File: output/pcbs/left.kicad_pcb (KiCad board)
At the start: 2 copper layers, 139.8 x 121.8 mm, 64 parts

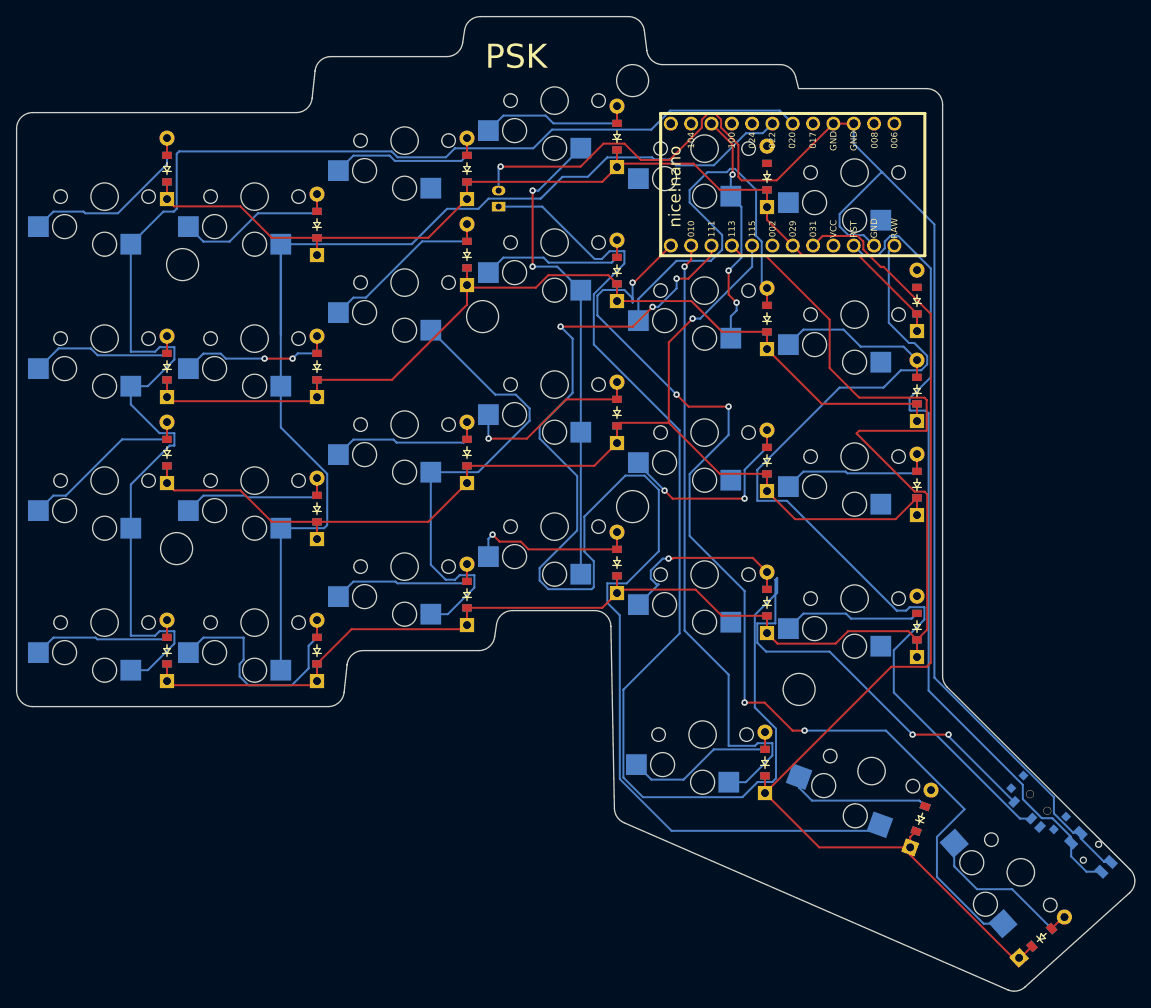
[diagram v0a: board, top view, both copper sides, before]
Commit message: clean slate, regenerated without trash routes
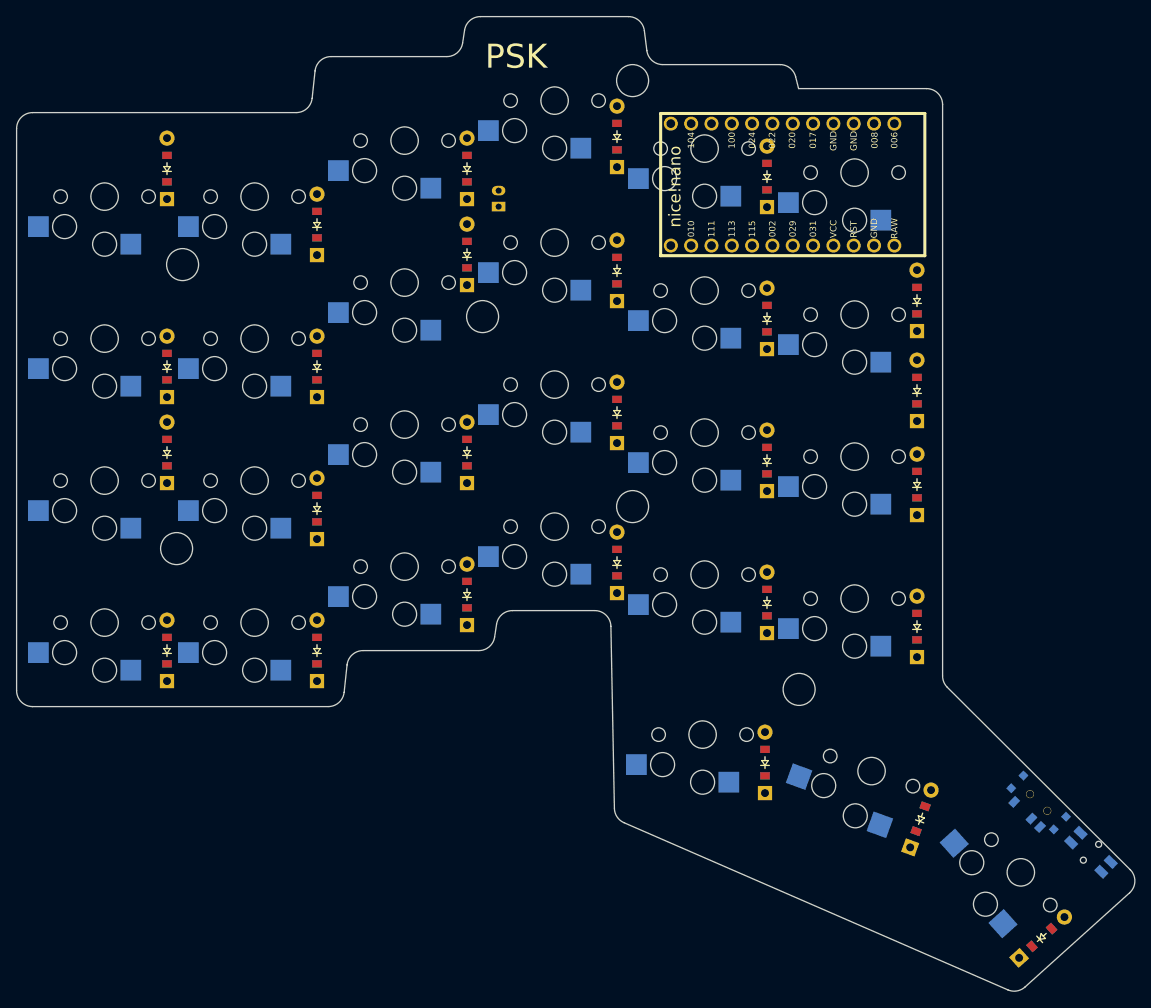
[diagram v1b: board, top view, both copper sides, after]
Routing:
- net pos: track 192.9 -> 0.00 mm, vias 2 -> 0
- net P113: track 192.4 -> 0.00 mm
- net GND: track 182.5 -> 0.00 mm, vias 1 -> 0
- net P020: track 173.7 -> 0.00 mm
- net P111: track 167.7 -> 0.00 mm, vias 3 -> 0
- net P115: track 144.3 -> 0.00 mm, vias 1 -> 0
- net P022: track 141.1 -> 0.00 mm
- net P031: track 138.5 -> 0.00 mm
- net P009: track 133.9 -> 0.00 mm, vias 5 -> 0
- net P029: track 119.5 -> 0.00 mm
- net P002: track 119.1 -> 0.00 mm
- net RAW: track 110.8 -> 0.00 mm
- net RST: track 102.8 -> 0.00 mm
- net P010: track 79.1 -> 0.00 mm, vias 1 -> 0
- net P100: track 60.5 -> 0.00 mm, vias 2 -> 0
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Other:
- outline, holes or cut-outs redrawn
- net class Default added: clearance 0.2, trace_width 0.25, via_dia 0.8, via_drill 0.4

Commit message: routed left, removed top left mounting hole from left and right and yaml
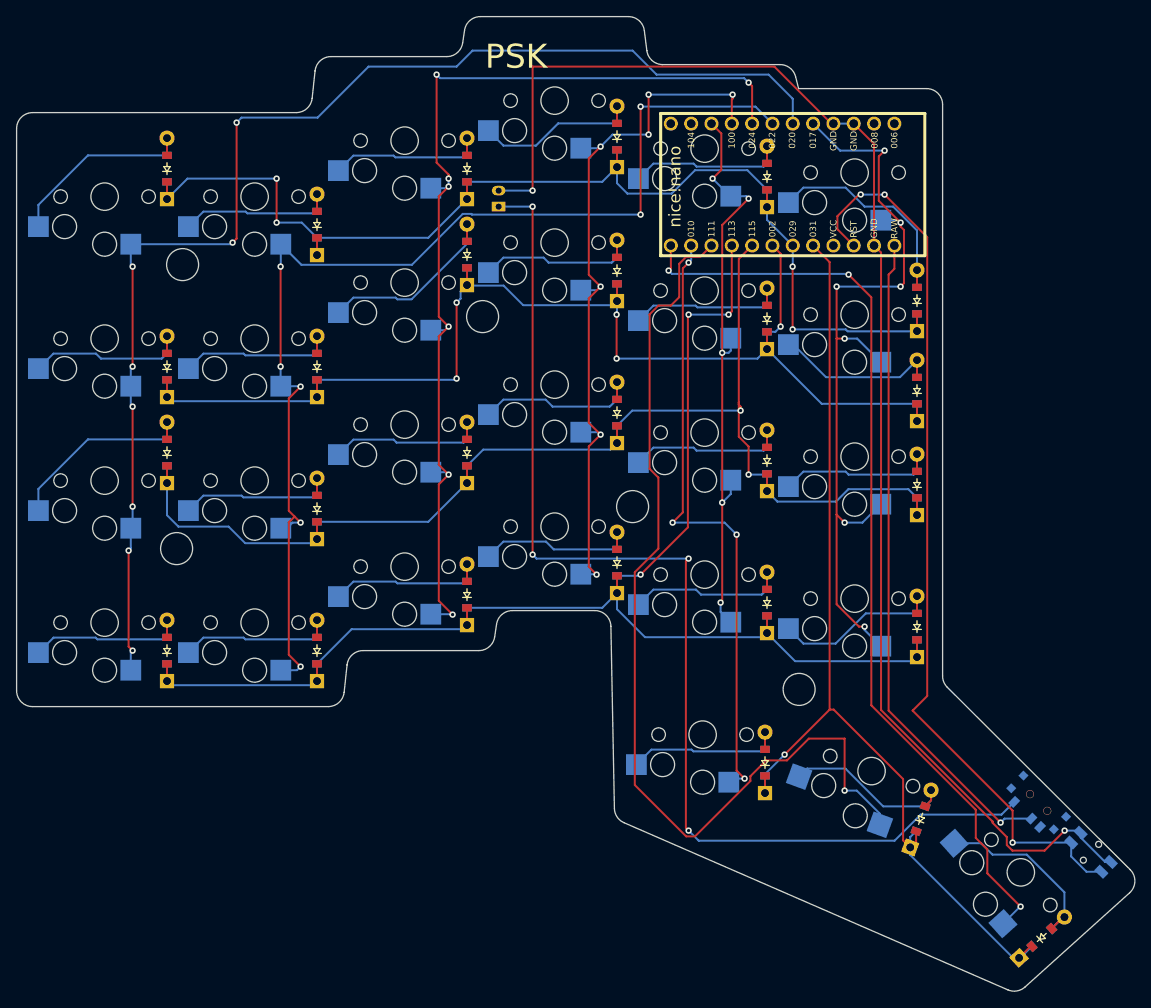
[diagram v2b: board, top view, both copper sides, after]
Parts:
- removed the ? at (166.0, 82.2)
- removed the ? at (186.8, 158.3)
- added ?: , HOLE_M2_TH, F.Cu at (186.8, 158.3)
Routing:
- net P113: track 0.00 -> 180.0 mm, vias 0 -> 3
- net GND: track 0.00 -> 177.2 mm, vias 0 -> 2
- net P115: track 0.00 -> 160.9 mm, vias 0 -> 2
- net P020: track 0.00 -> 160.9 mm, vias 0 -> 8
- net P002: track 0.00 -> 155.5 mm, vias 0 -> 5
- net P029: track 0.00 -> 148.1 mm, vias 0 -> 4
- net pos: track 0.00 -> 145.0 mm, vias 0 -> 4
- net P022: track 0.00 -> 143.2 mm, vias 0 -> 7
- net P024: track 0.00 -> 125.9 mm, vias 0 -> 7
- net P031: track 0.00 -> 125.5 mm, vias 0 -> 1
- net P111: track 0.00 -> 122.0 mm, vias 0 -> 1
- net P009: track 0.00 -> 116.9 mm, vias 0 -> 3
- net RST: track 0.00 -> 114.3 mm, vias 0 -> 3
- net P017: track 0.00 -> 101.0 mm, vias 0 -> 7
- net P100: track 0.00 -> 92.6 mm, vias 0 -> 7
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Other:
- outline, holes or cut-outs redrawn
- net class Default removed

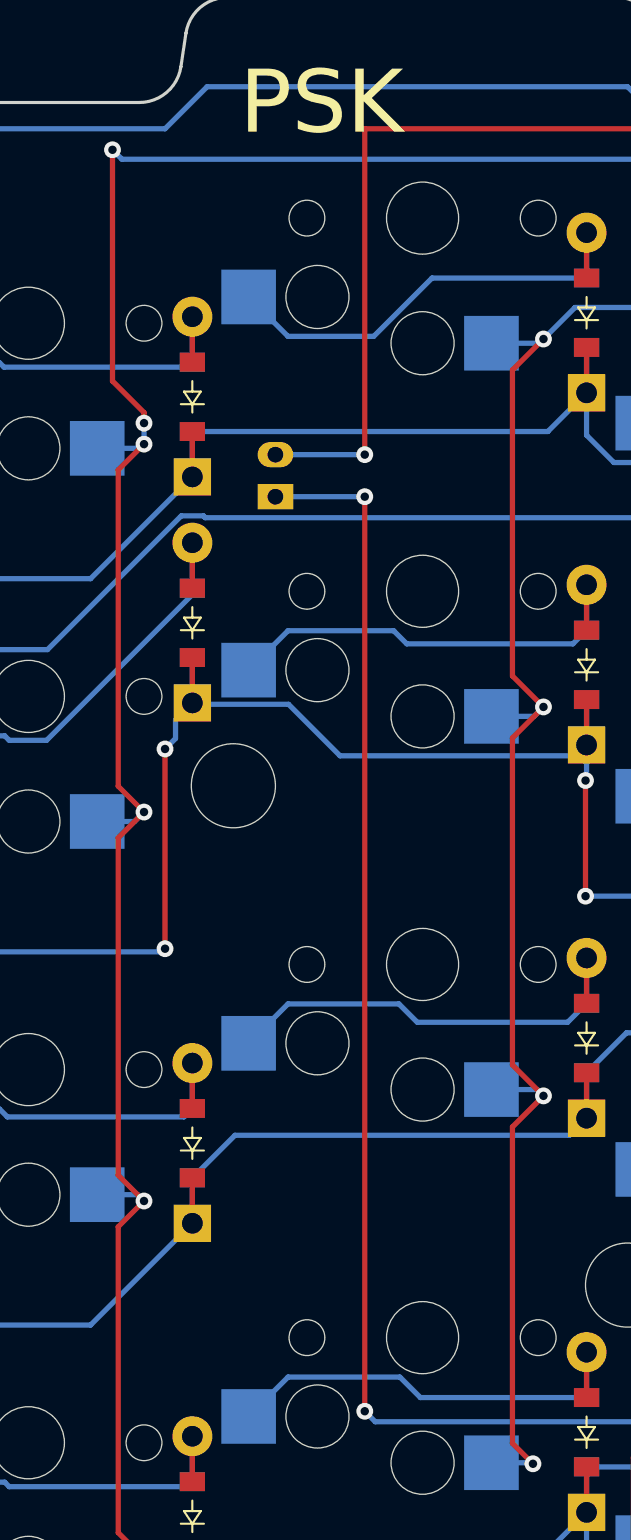
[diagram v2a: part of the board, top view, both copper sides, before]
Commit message: routed left and right, DRC passed
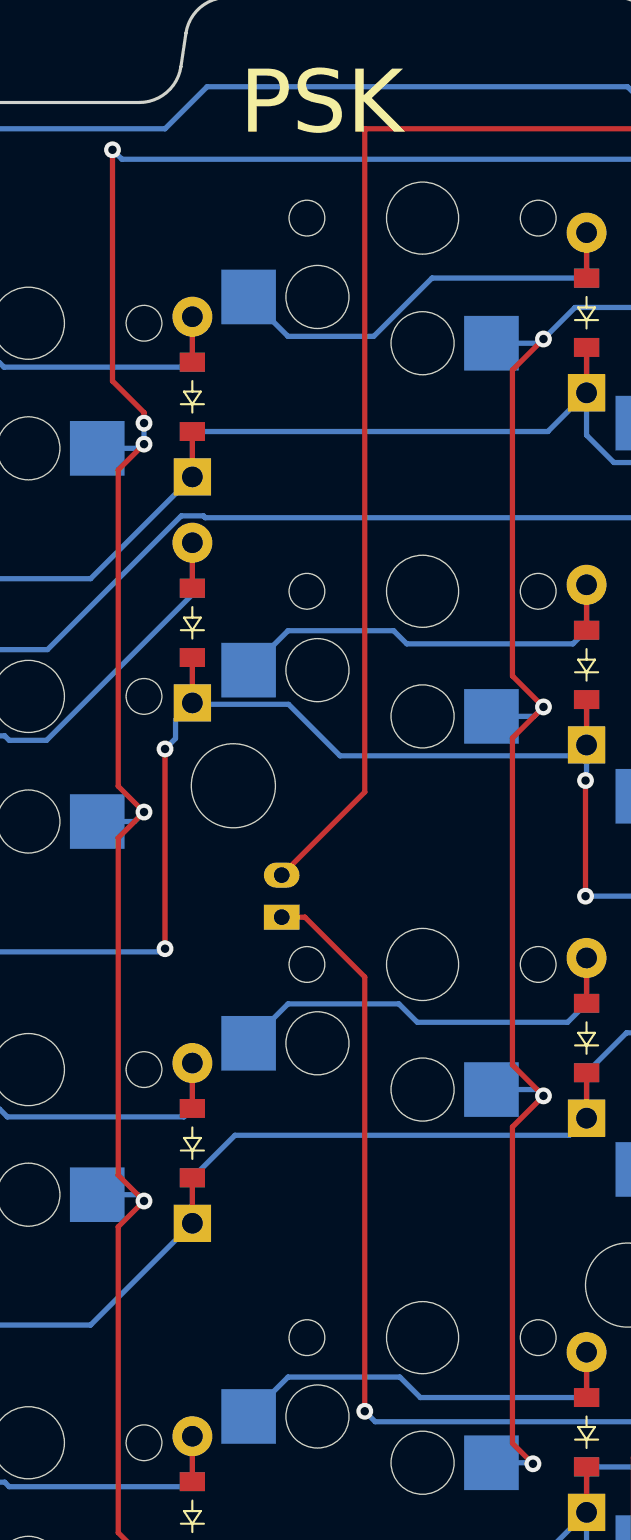
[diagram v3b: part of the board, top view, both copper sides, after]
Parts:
- moved JST1 20.0 mm to (149.6, 117.0)
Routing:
- net pos: track 145.0 -> 123.0 mm, vias 4 -> 3
- net GND: track 177.2 -> 194.6 mm, vias 2 -> 1
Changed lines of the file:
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@@
 	(footprint "JST_PH_S2B-PH-K_02x2.00mm_Angled"
 		(layer "F.Cu")
-		(at 149.25 97 90)
+		(at 149.55 117 90)
 		(descr "JST PH series connector, S2B-PH-K, side entry type, through hole, Datasheet: http://www.jst-mfg.com/product/pdf/eng/ePH.pdf")
 		(tags "connector jst ph")
@@
 	)
 	(segment
-		(start 183.717257 80.5)
-		(end 190.847257 87.63)
-		(width 0.25)
-		(layer "F.Cu")
-		(net 43)
-	)
-	(segment
 		(start 196.18 90.17)
 		(end 196.18 102.87)
@@
 	)
 	(segment
-		(start 153.5 96)
+		(start 153.5 112.05)
 		(end 153.5 80.5)
 		(width 0.25)
@@
 	)
 	(segment
-		(start 153.5 80.5)
-		(end 183.717257 80.5)
+		(start 183.717257 80.5)
+		(end 190.847257 87.63)
 		(width 0.25)
 		(layer "F.Cu")
@@
 	)
 	(segment
-		(start 211 174.863604)
-		(end 211 175.025305)
+		(start 149.55 116)
+		(end 153.5 112.05)
 		(width 0.25)
 		(layer "F.Cu")
@@
 	)
 	(segment
-		(start 212.775 177.800305)
-		(end 213.474695 178.5)
+		(start 153.5 80.5)
+		(end 183.717257 80.5)
 		(width 0.25)
 		(layer "F.Cu")
@@
 	)
 	(segment
-		(start 211 175.025305)
-		(end 212.775 176.800305)
+		(start 190.847257 87.63)
+		(end 191.1 87.63)
 		(width 0.25)
 		(layer "F.Cu")
@@
 	)
 	(segment
-		(start 190.847257 87.63)
-		(end 191.1 87.63)
+		(start 211 174.863604)
+		(end 211 175.025305)
 		(width 0.25)
 		(layer "F.Cu")
 		(net 43)
 	)
-	(via
-		(at 220 176)
-		(size 0.8)
-		(drill 0.4)
-		(layers "F.Cu" "B.Cu")
+	(segment
+		(start 212.775 177.800305)
+		(end 213.474695 178.5)
+		(width 0.25)
+		(layer "F.Cu")
+		(net 43)
+	)
+	(segment
+		(start 211 175.025305)
+		(end 212.775 176.800305)
+		(width 0.25)
+		(layer "F.Cu")
 		(net 43)
 	)
 	(via
-		(at 153.5 96)
+		(at 220 176)
 		(size 0.8)
 		(drill 0.4)
@@
 	)
 	(segment
-		(start 149.25 96)
-		(end 153.5 96)
-		(width 0.25)
-		(layer "B.Cu")
-		(net 43)
-	)
-	(segment
 		(start 191.1 87.63)
 		(end 193.64 87.63)
@@
 	)
 	(segment
-		(start 153.5 98)
-		(end 153.5 141.5)
+		(start 150.65 118)
+		(end 149.55 118)
 		(width 0.25)
 		(layer "F.Cu")
@@
 	)
 	(segment
+		(start 153.5 141.5)
+		(end 153.5 120.85)
+		(width 0.25)
+		(layer "F.Cu")
+		(net 50)
+	)
+	(segment
+		(start 153.5 120.85)
+		(end 150.65 118)
+		(width 0.25)
+		(layer "F.Cu")
+		(net 50)
+	)
+	(segment
 		(start 173 142)
 		(end 172.6605 142.3395)
@@
 	)
 	(via
-		(at 153.5 98)
-		(size 0.8)
-		(drill 0.4)
-		(layers "F.Cu" "B.Cu")
-		(net 50)
-	)
-	(via
 		(at 153.5 141.5)
 		(size 0.8)
@@
 		(width 0.25)
 		(layer "B.Cu")
-		(net 50)
-	)
-	(segment
-		(start 149.25 98)
-		(end 153.5 98)
-		(width 0.25)
-		(layer "B.Cu")

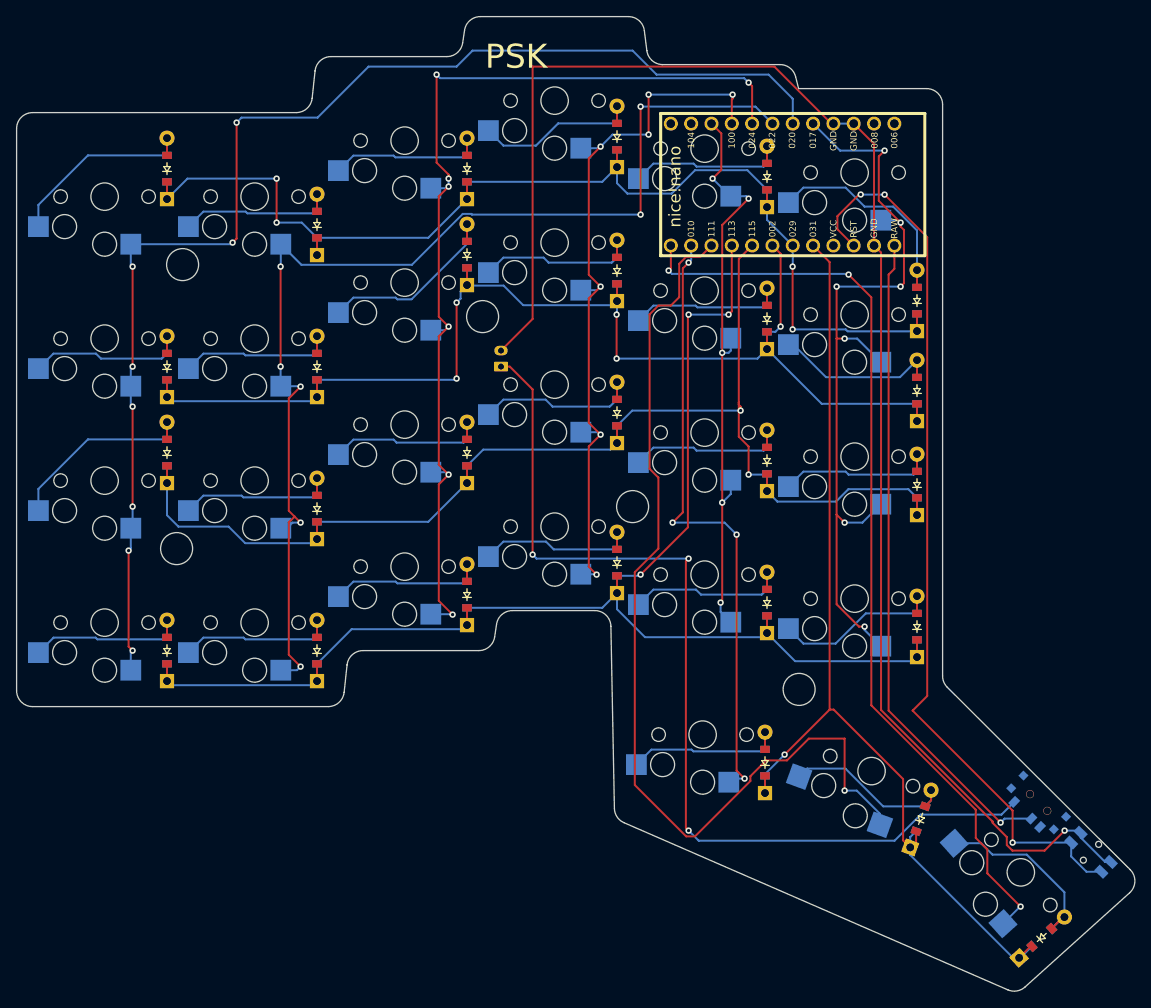
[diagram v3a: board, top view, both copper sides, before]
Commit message: generated gerber files, sent off for fab
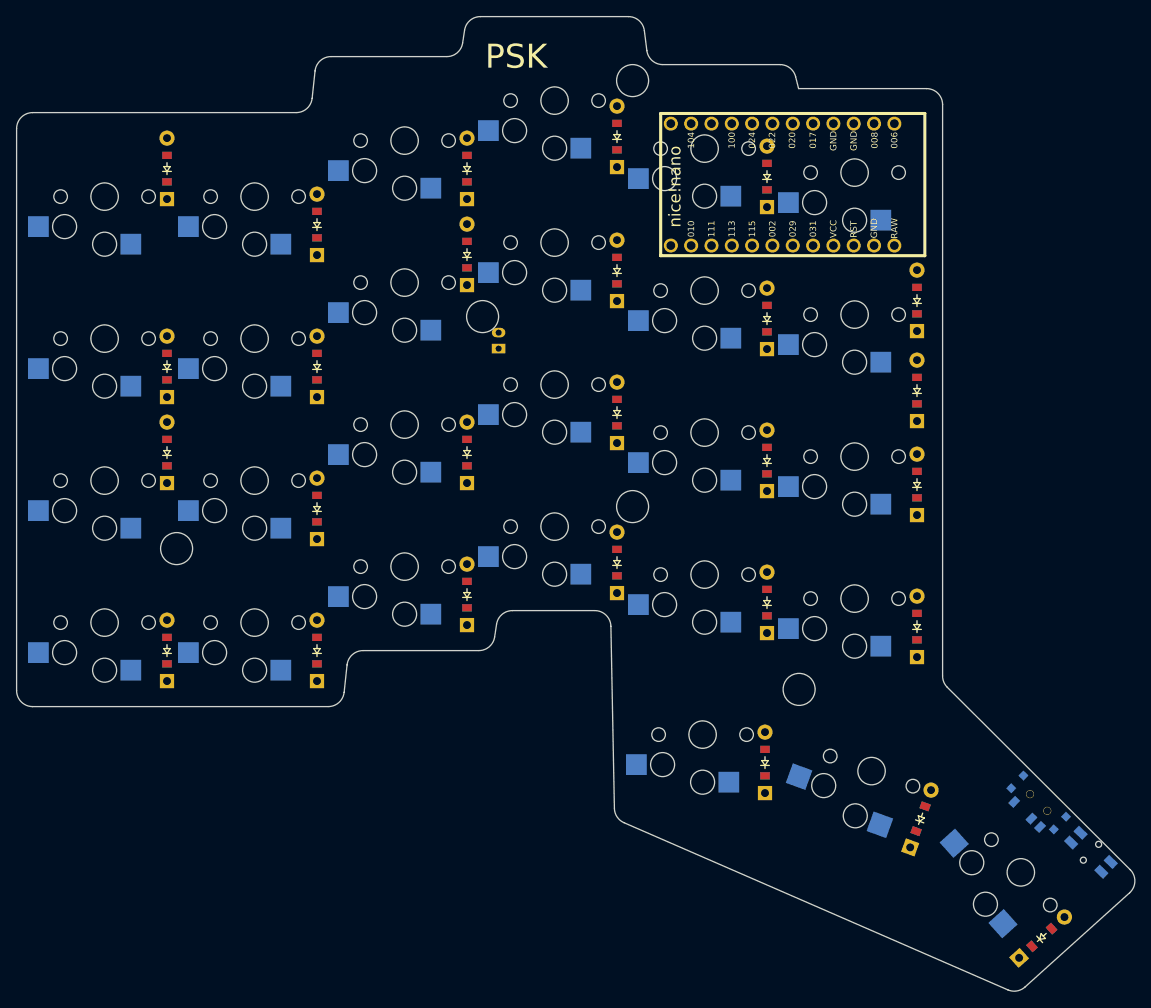
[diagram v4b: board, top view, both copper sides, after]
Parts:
- removed the ? at (109.8, 105.2)
- removed the ? at (186.8, 158.3)
- added ?: , HOLE_M2_TH, F.Cu at (166.0, 82.2)
- added ?: , HOLE_M2_TH, F.Cu at (186.8, 158.3)
- moved JST1 2.27 mm to (149.2, 114.8)
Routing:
- net GND: track 194.6 -> 0.00 mm, vias 1 -> 0
- net P113: track 180.0 -> 0.00 mm, vias 3 -> 0
- net P115: track 160.9 -> 0.00 mm, vias 2 -> 0
- net P020: track 160.9 -> 0.00 mm, vias 8 -> 0
- net P002: track 155.5 -> 0.00 mm, vias 5 -> 0
- net P029: track 148.1 -> 0.00 mm, vias 4 -> 0
- net P022: track 143.2 -> 0.00 mm, vias 7 -> 0
- net P024: track 125.9 -> 0.00 mm, vias 7 -> 0
- net P031: track 125.5 -> 0.00 mm, vias 1 -> 0
- net pos: track 123.0 -> 0.00 mm, vias 3 -> 0
- net P111: track 122.0 -> 0.00 mm, vias 1 -> 0
- net P009: track 116.9 -> 0.00 mm, vias 3 -> 0
- net RST: track 114.3 -> 0.00 mm, vias 3 -> 0
- net P017: track 101.0 -> 0.00 mm, vias 7 -> 0
- net P100: track 92.6 -> 0.00 mm, vias 7 -> 0
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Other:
- outline, holes or cut-outs redrawn
- net class Default added: clearance 0.2, trace_width 0.25, via_dia 0.8, via_drill 0.4
